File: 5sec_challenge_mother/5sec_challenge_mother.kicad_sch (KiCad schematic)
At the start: 7 parts, among them J1 Conn_01x07_Socket, J2 Barrel_Jack_Switch, U1 L7805

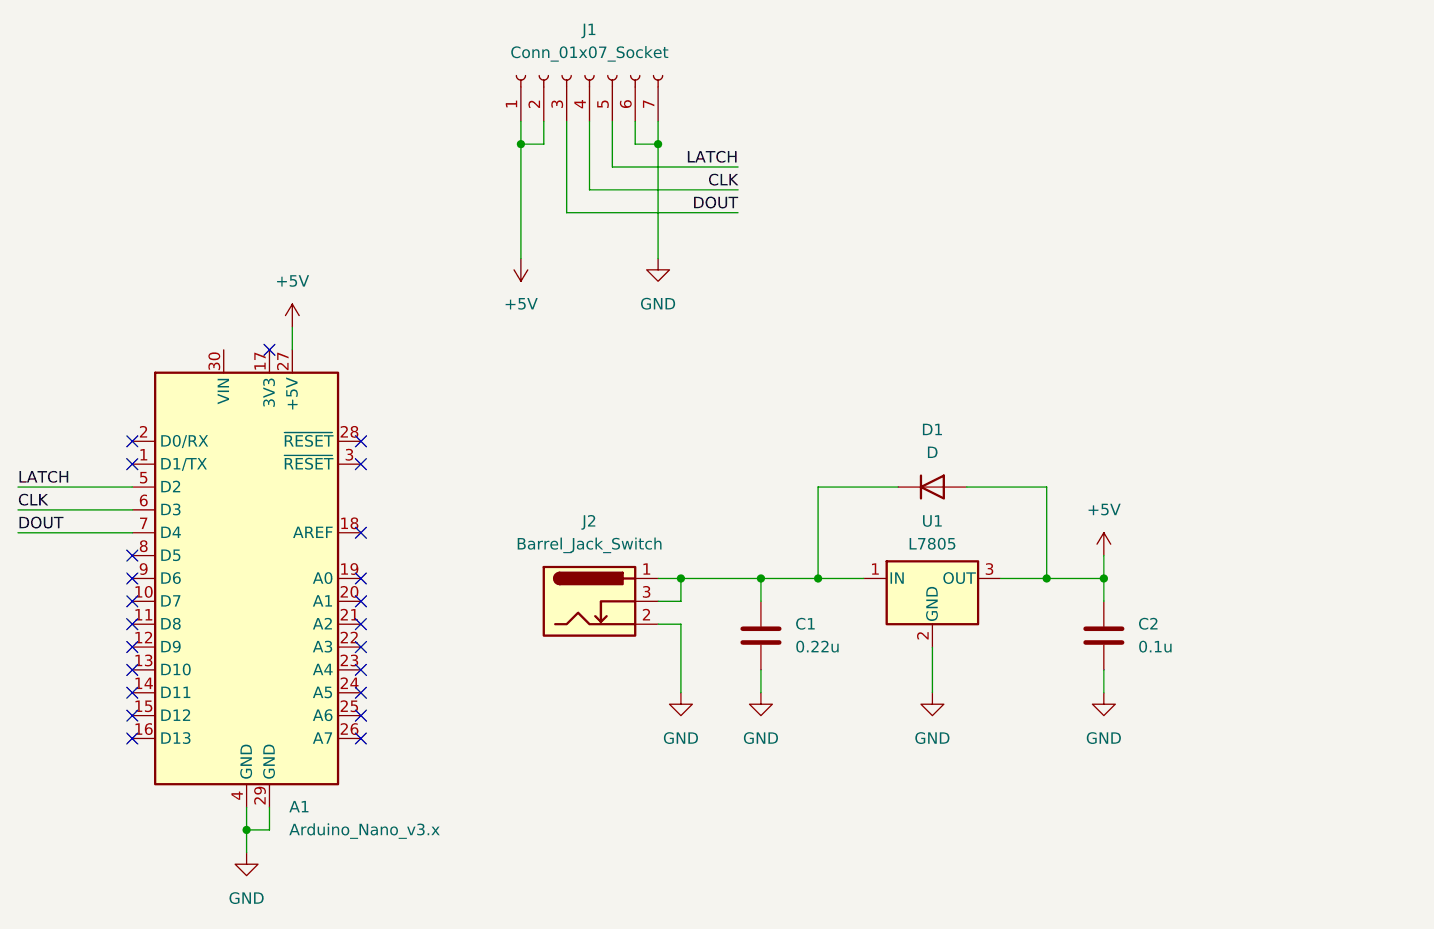
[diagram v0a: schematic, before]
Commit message: スイッチ付け忘れてたので追加
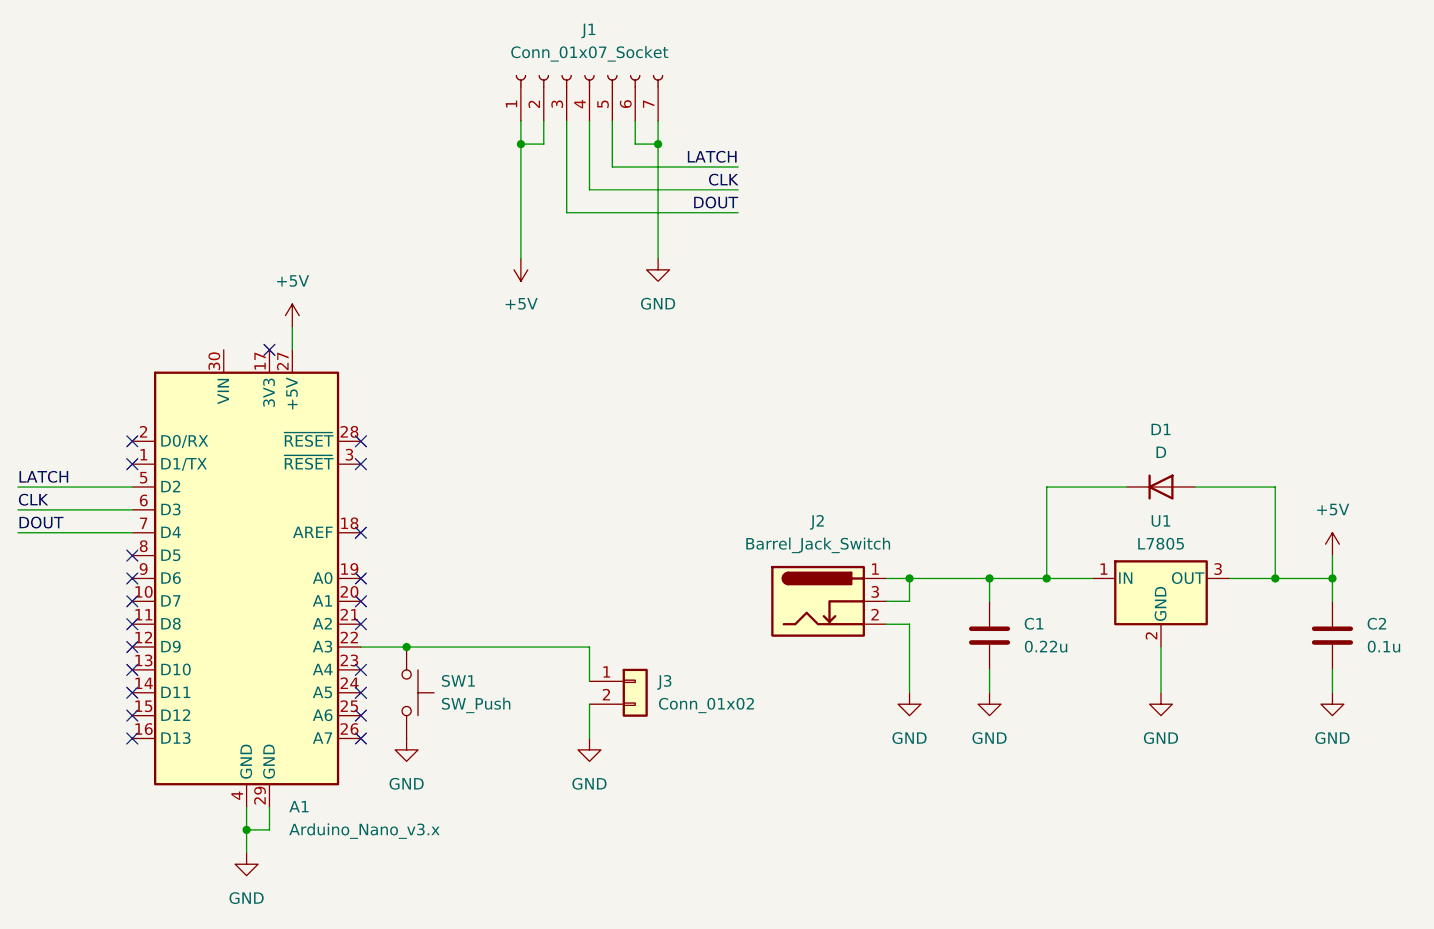
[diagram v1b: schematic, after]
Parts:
- added J3: Conn_01x02, Connector_JST:JST_XH_B2B-XH-AM_1x02_P2.50mm_Vertical, symbol Connector_Generic:Conn_01x02
- added SW1: SW_Push, Button_Switch_THT:SW_PUSH_6mm, symbol Switch:SW_Push
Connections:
- net GND: now also J3.2 (Pin_2), SW1.2
- net at A1.22 (A3): now also J3.1 (Pin_1), SW1.1
- no-connect marks 23 -> 22
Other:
- moved on the sheet: C1, C2, D1, J2, U1
